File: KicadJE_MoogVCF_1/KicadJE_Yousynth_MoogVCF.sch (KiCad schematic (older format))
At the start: 99 parts, among them J201 CV2, J202 Input2, J203 CV1, J204 Out VCF, J205 Input1, P201 Doepfer_Power_10pin, Q201 UMX1N, Q202 SS9014, Q203 SS9014, Q204 SS9014, Q205 SS9014, Q206 SS9014, Q207 SS9014, Q208 UMX1N, Q209 UMX1N, Q210 UMX1N, Q211 SS9014, Q212 SS9015, U201 TL072

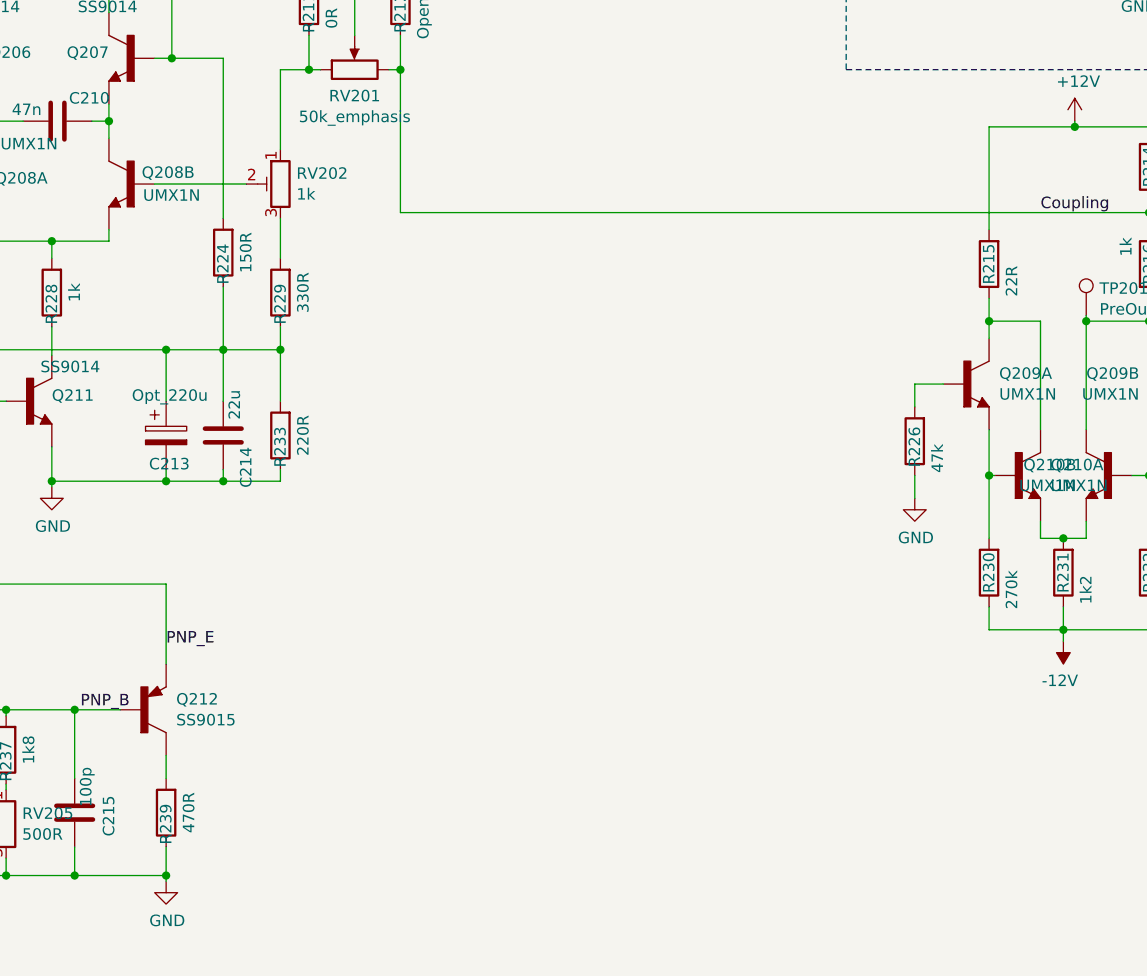
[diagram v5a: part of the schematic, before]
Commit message: forgot a trimmer
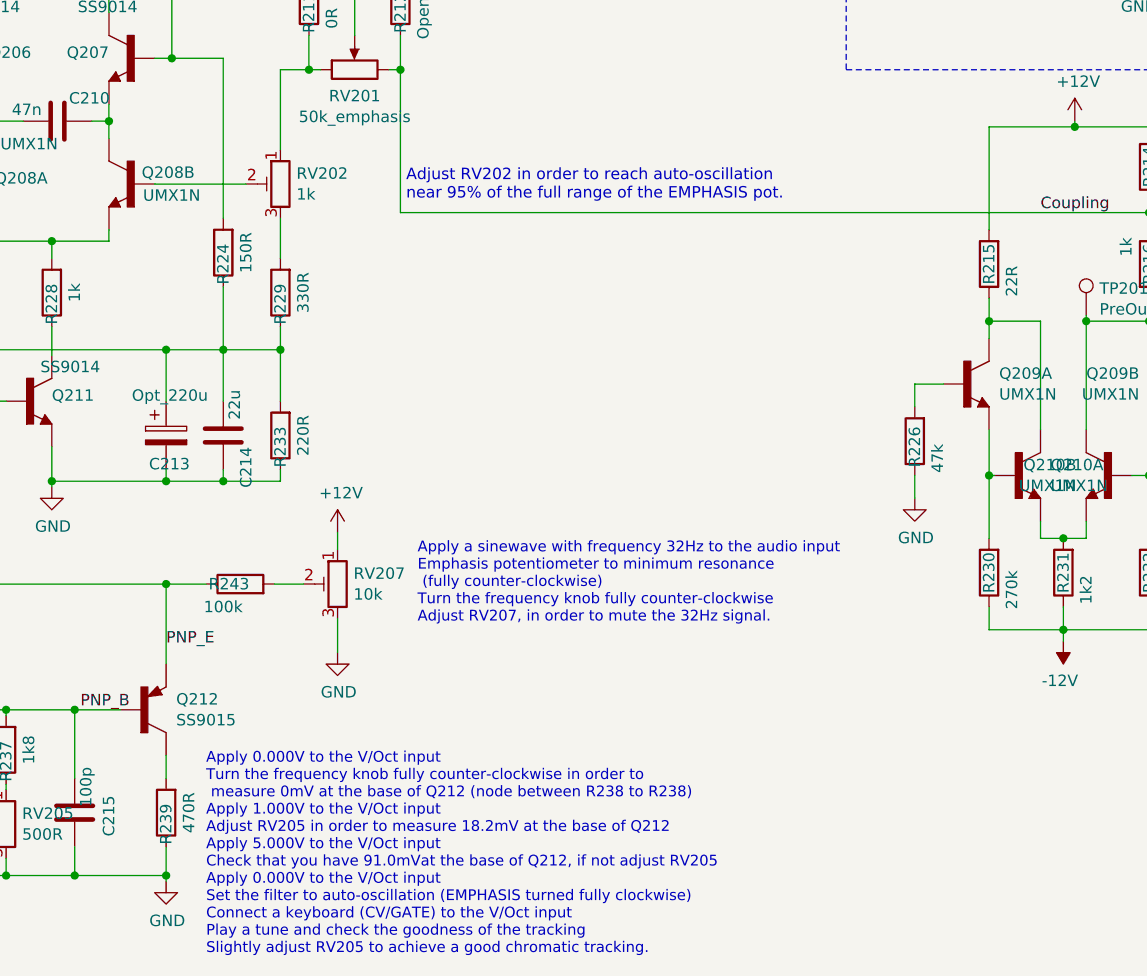
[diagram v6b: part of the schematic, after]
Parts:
- added R243: 100k, Resistor_SMD:R_0805_2012Metric_Pad1.15x1.40mm_HandSolder, symbol Device:R
- added RV207: 10k, AJ-Dropbox-Kicad:Bourns3296WV, symbol Device:R_POT_TRIM
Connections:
- net +12V: now also RV207.1
- net GND: now also RV207.3
- net PNP_E: now also R243.1
- new net: R243.2, RV207.2
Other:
- note added: "Adjust RV202 in order to reach auto-oscillation \nnear 95% of the full range of the EMPHASIS pot."
- note added: "Apply 0.000V to the V/Oct input\nTurn the frequency knob fully counter-clockwise in order to\n measure 0mV at the base of Q212 (node between R238 to R238)\nApply 1.000V to the V/Oct input\nAdjust RV205 in order to measure 18.2mV at the base of Q212\nApply 5.000V to the V/Oct input\nCheck that you have 91.0mVat the base of Q212, if not adjust RV205\nApply 0.000V to the V/Oct input\nSet the filter 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"
- note added: "Apply a sinewave with frequency 32Hz to the audio input\nEmphasis potentiometer to minimum resonance\n (fully counter-clockwise)\nTurn the frequency knob fully counter-clockwise\nAdjust RV207, in order to mute the 32Hz signal."
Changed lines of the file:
@@
 Wire Wire Line
 	3150 6550 3525 6550
+$Comp
+L Device:R_POT_TRIM RV207
+U 1 1 5F021A79
+P 4975 6000
+F 0 "RV207" H 4905 6046 50  0000 R CNN
+F 1 "10k" H 4905 5955 50  0000 R CNN
+F 2 "AJ-Dropbox-Kicad:Bourns3296WV" H 4975 6000 50  0001 C CNN
+F 3 "~" H 4975 6000 50  0001 C CNN
+	1    4975 6000
+	-1   0    0    -1
+$EndComp
+$Comp
+L power:GND #PWR?
+U 1 1 5F022297
+P 4975 6300
+AR Path="/5D99B81E/5F022297" Ref="#PWR?"  Part="1"
+AR Path="/5D99B7BA/5F022297" Ref="#PWR0217"  Part="1"
+F 0 "#PWR0217" H 4975 6050 50  0001 C CNN
+F 1 "GND" H 4980 6127 50  0000 C CNN
+F 2 "" H 4975 6300 50  0001 C CNN
+F 3 "" H 4975 6300 50  0001 C CNN
+	1    4975 6300
+	1    0    0    -1
+$EndComp
+$Comp
+L Device:R R?
+U 1 1 5F02266F
+P 4550 6000
+AR Path="/5D99B81E/5F02266F" Ref="R?"  Part="1"
+AR Path="/5D99B7BA/5F02266F" Ref="R243"  Part="1"
+F 0 "R243" V 4550 6050 50  0000 C CNN
+F 1 "100k" V 4450 6075 50  0000 C CNN
+F 2 "Resistor_SMD:R_0805_2012Metric_Pad1.15x1.40mm_HandSolder" V 4480 6000 50  0001 C CNN
+F 3 "~" H 4550 6000 50  0001 C CNN
+	1    4550 6000
+	0    -1   -1   0
+$EndComp
+Wire Wire Line
+	4225 6000 4400 6000
+Wire Wire Line
+	4700 6000 4825 6000
+Connection ~ 4225 6000
+Wire Wire Line
+	4975 6300 4975 6150
+$Comp
+L power:+12V #PWR?
+U 1 1 5F06322A
+P 4975 5775
+AR Path="/5D99B81E/5F06322A" Ref="#PWR?"  Part="1"
+AR Path="/5D99B7BA/5F06322A" Ref="#PWR0216"  Part="1"
+F 0 "#PWR0216" H 4975 5625 50  0001 C CNN
+F 1 "+12V" H 4990 5948 50  0000 C CNN
+F 2 "" H 4975 5775 50  0001 C CNN
+F 3 "" H 4975 5775 50  0001 C CNN
+	1    4975 5775
+	1    0    0    -1
+$EndComp
+Wire Wire Line
+	4975 5850 4975 5775
+Text Notes 5325 6175 0    47   ~ 0
+Apply a sinewave with frequency 32Hz to the audio input\nEmphasis potentiometer to minimum resonance\n (fully counter-clockwise)\nTurn the frequency knob fully counter-clockwise\nAdjust RV207, in order to mute the 32Hz signal.
+Text Notes 5275 4325 0    50   ~ 0
+Adjust RV202 in order to reach auto-oscillation \nnear 95% of the full range of the EMPHASIS pot.
+Text Notes 4400 7625 0    47   ~ 0
+Apply 0.000V to the V/Oct input\nTurn the frequency knob fully counter-clockwise in order to\n measure 0mV at the base of Q212 (node between R238 to R238)\nApply 1.000V to the V/Oct input\nAdjust RV205 in order to measure 18.2mV at the base of Q212\nApply 5.000V to the V/Oct input\nCheck that you have 91.0mVat the base of Q212, if not adjust RV205\nApply 0.000V to the V/Oct input\nSet the filter to auto-oscillation (EMPHASIS turned fully clockwise)\nConnect a keyboard (CV/GATE) to the V/Oct input\nPlay a tune and check the goodness of the tracking\nSlightly adjust RV205 to achieve a good chromatic tracking.
 $EndSCHEMATC
